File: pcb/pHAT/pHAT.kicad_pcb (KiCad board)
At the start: 2 copper layers, 65 x 30 mm, 45 parts, among them M1 mount1, M2 mount1, M3 mount1, M4 mount1, P2 USB_A, P4 CONN_01X30, Q1 XTL, U1 FE1.1S, U2 ATTINY102, m1 mount2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

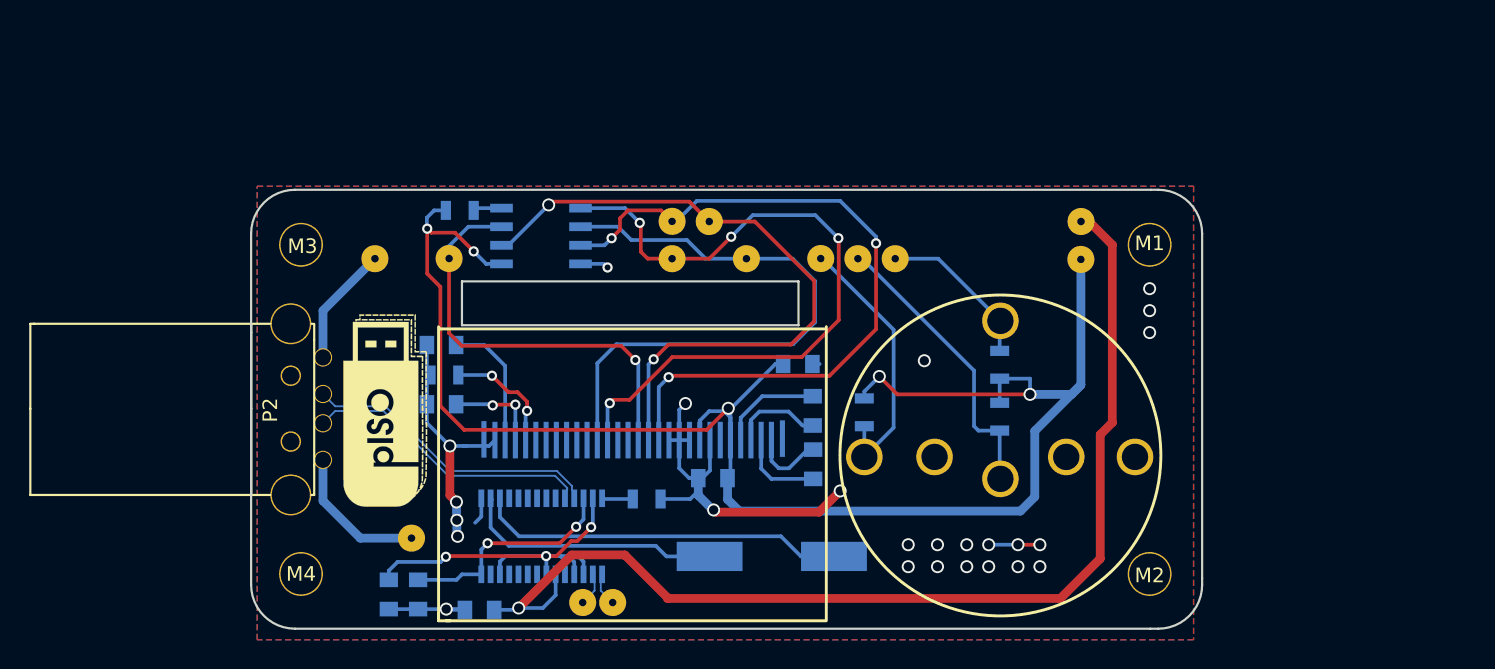
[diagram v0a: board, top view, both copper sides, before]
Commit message: PCB layout with buttons
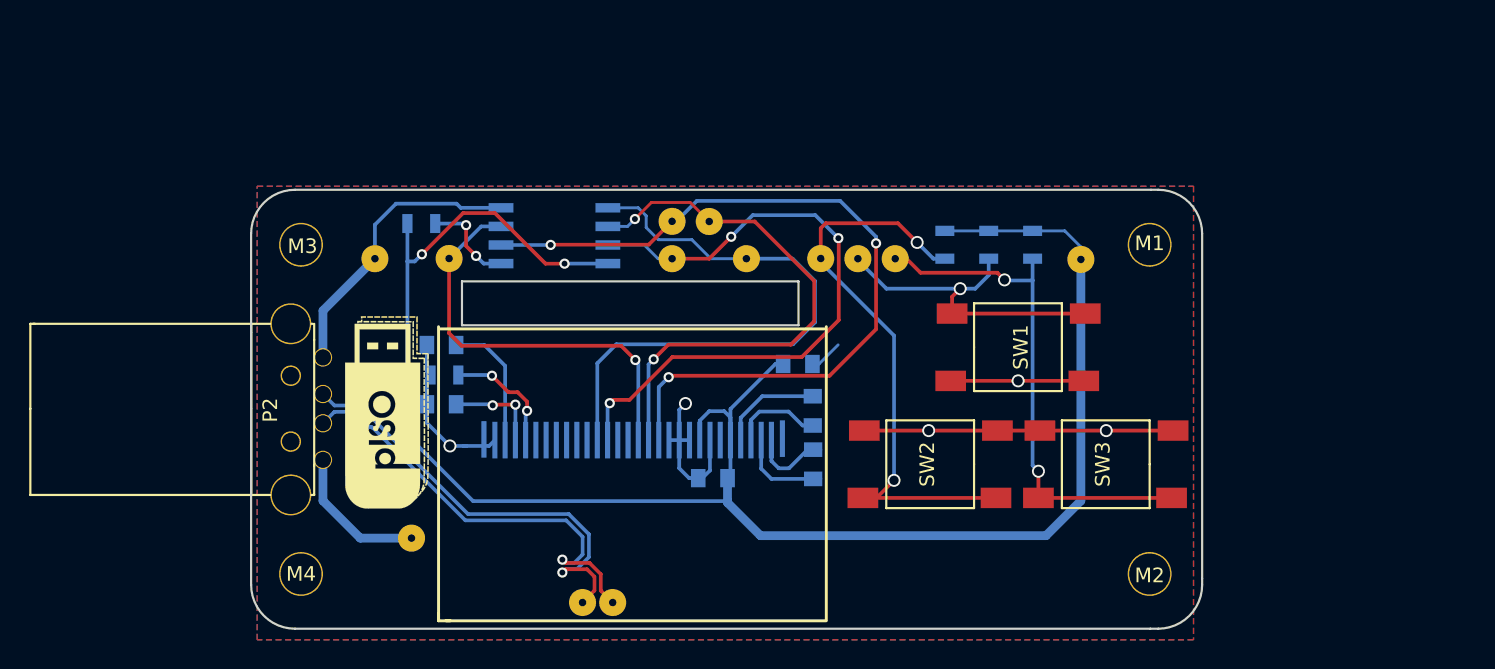
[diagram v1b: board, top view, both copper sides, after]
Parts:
- removed the G*** at (118.7, 94.6)
- removed Q1: XTL, Crystals:Crystal_SMD_HC49-SD
- removed R4: 2.7K, Resistors_SMD:R_0805
- removed U2: ATTINY102, Housings_SOIC:SOIC-8_3.9x4.9mm_Pitch1.27mm
- removed VCC2, VCC3, VCC4: 10uF, Capacitors_SMD:C_0805
- removed W1: NO, pISO:swpins
- removed W2: A, pISO:swpins
- removed W3: B, pISO:swpins
- removed W4: COM, pISO:swpins
- removed W6: VDD5, pISO:SLP
- removed m1: mount2, pISO:swpins
- removed m2: mount1, pISO:swpins
- added G***: LOGO, pISO:LOGO, F.Cu at (118.8, 94.7)
- added SW1: SW_Push, pISO:spst, F.Cu at (161.9, 90.3)
- added SW2: SW_Push, pISO:spst, F.Cu at (155.9, 98.3)
- added SW3: SW_Push, pISO:spst, F.Cu at (167.9, 98.3)
- U1: value FE1.1S -> ATTINY25/45/85; footprint Housings_SSOP:SSOP-28_3.9x9.9mm_Pitch0.635mm -> Housings_SOIC:SOIJ-8_5.3x5.3mm_Pitch1.27mm
- moved U1 20.6 mm to (130.2, 82.6), turned to 0 degrees
- moved R2 12.7 mm to (156.9, 83.3)
- moved R1 11.8 mm to (159.9, 83.3)
- moved R3 8.50 mm to (162.9, 83.3), turned to 270 degrees
- moved R5 2.78 mm to (121.1, 81.8), turned to 0 degrees
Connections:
- D+ pad 1: /D_P -> /DM1_P
- D- pad 1: /D_N -> /DM1_N
- P4 pad 15: /D/C -> /DC
- R5 pad 1: Net-(R5-Pad1) -> +3V3
- R5 pad 2: +3V3 -> Net-(R5-Pad2)
- U1 pad 1: GND -> Net-(R5-Pad2)
- U1 pad 2: /XOUT -> /CS
- U1 pad 3: /XIN -> /DC
- U1 pad 4: (no net) -> GND
- U1 pad 5: (no net) -> /MOSI
- U1 pad 6: (no net) -> /RST
- U1 pad 7: (no net) -> /SCLK
- U1 pad 8: /DM2_N -> +3V3
- W11 pad 1: /D/C -> /DC
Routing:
- net /VDD5: track 74.3 -> 0.00 mm, vias 1 -> 0
- net /3V3_O: track 30.2 -> 0.00 mm, vias 3 -> 0
- net /D/C: track 29.1 -> 0.00 mm, vias 1 -> 0
- net /DC: track 0.00 -> 28.6 mm, vias 0 -> 1
- net /XIN: track 25.2 -> 0.00 mm
- net Net-(B1-Pad1): track 11.0 -> 35.7 mm, vias 0 -> 2
- net Net-(A1-Pad1): track 18.7 -> 41.6 mm, vias 0 -> 2
- net /XOUT: track 17.9 -> 0.00 mm
- net /1V8: track 15.5 -> 0.00 mm, vias 2 -> 0
- net GND: track 63.8 -> 74.5 mm, vias 9 -> 5
- net /DM1_P: track 20.5 -> 30.6 mm, vias 0 -> 1
- net /DM1_N: track 20.6 -> 30.6 mm, vias 0 -> 1
- net /RST: track 45.3 -> 37.5 mm
- net Net-(R5-Pad2): track 0.00 -> 6.46 mm, vias 0 -> 2
- net +3V3: track 118.9 -> 124.7 mm, vias 5 -> 2
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
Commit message: update for USBA board
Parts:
- added W1: ExtraPOGO, pISO:SLP, F.Cu at (167.4, 105.8)
- added W2: ExtraPOGO, pISO:SLP, F.Cu at (116.4, 105.8)
- R1, R2, R3: value 50k -> 10k
- moved SW1 7.63 mm to (155.5, 94.4)
- moved SW2 5.37 mm to (155.4, 103.6), turned to 90 degrees
- moved SW3 0.79 mm to (167.7, 99.0)
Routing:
- net GND: track 74.5 -> 52.9 mm, vias 5 -> 6
- net Net-(B1-Pad1): track 35.7 -> 40.5 mm, vias 2 -> 1
- net Net-(NO1-Pad1): track 23.0 -> 26.9 mm
- net Net-(A1-Pad1): track 41.6 -> 42.5 mm

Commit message: usbc
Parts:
- removed P2: USB_A, pISO:usb
- added U2: USBC, pISO:USBC, F.Cu at (123.9, 83.3)
- moved IREF1 20.8 mm to (140.6, 81.4)
- moved W5 20.8 mm to (138.3, 92.6)
- moved W12 20.8 mm to (135.8, 73.5)
- moved A1 20.8 mm to (166.3, 73.5)
- moved C1 20.8 mm to (165.8, 87.5)
- moved C2 20.8 mm to (165.8, 83.9)
- moved M1 20.8 mm to (188.8, 72.5)
- moved M2 20.8 mm to (188.8, 95.0)
- moved M3 20.8 mm to (130.8, 72.5)
- moved M4 20.8 mm to (130.8, 95.0)
- moved R1 20.8 mm to (177.8, 72.5)
- moved R2 20.8 mm to (174.8, 72.5)
- moved R3 20.8 mm to (180.8, 72.5)
- moved R5 20.8 mm to (139.0, 71.1)
- moved SW1 20.8 mm to (173.4, 83.7)
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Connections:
- W5 pad 1: Net-(P2-Pad1) -> /piPOWER
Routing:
- net /piPOWER: track 0.00 -> 67.7 mm, vias 0 -> 1
- net /DM1_P: track 30.6 -> 55.6 mm, vias 1 -> 2
- net /DM1_N: track 30.6 -> 54.1 mm, vias 1 -> 2
- net GND: track 52.9 -> 75.0 mm, vias 6 -> 8
- net Net-(P2-Pad1): track 9.91 -> 0.00 mm
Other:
- board size 65 x 30 mm -> 71.9 x 30 mm
- board text added: "DOWN"
- board text added: "SELECT"
- board text added: "UP"
